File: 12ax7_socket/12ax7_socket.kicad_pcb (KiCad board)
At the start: 2 copper layers, 24.1 x 29.8 mm, 2 parts, among them J1 Conn_01x09, U1 ECC83

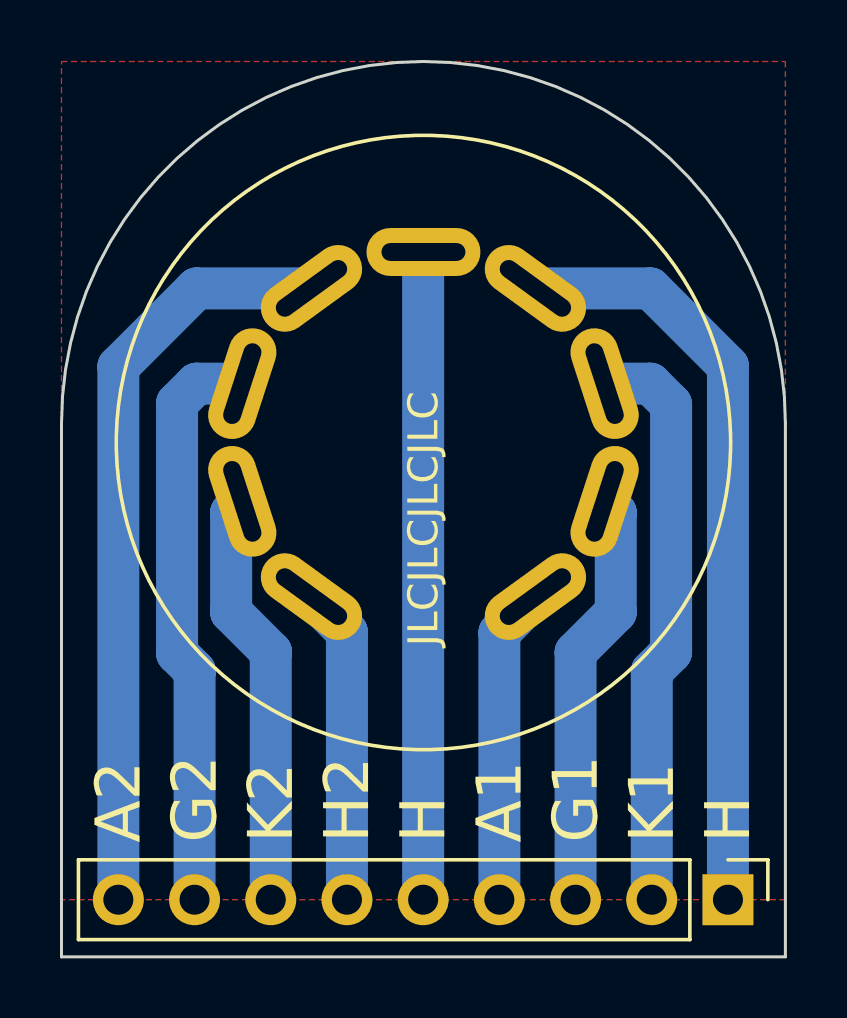
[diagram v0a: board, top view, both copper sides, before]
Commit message: Fix footprint of valve socket
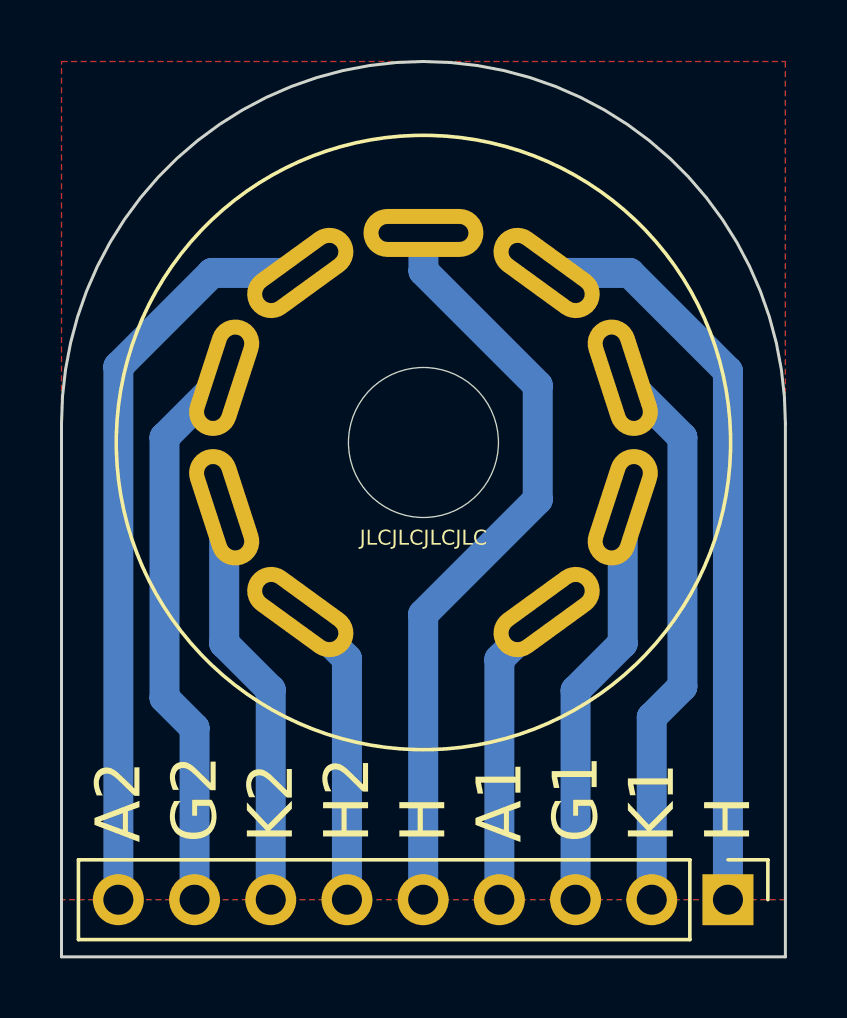
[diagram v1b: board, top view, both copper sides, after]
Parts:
- U1: footprint tube_breakouts:Valve_12AX7_Socket -> kosmo-lib:Valve_12AX7_Socket
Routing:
- net /H3: track 21.6 -> 25.4 mm
- net /K1: track 19.3 -> 18.6 mm
- net /G2: track 19.2 -> 18.6 mm
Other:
- board text added: "12AX7"
- board text removed: "12AX7 ECC83"
